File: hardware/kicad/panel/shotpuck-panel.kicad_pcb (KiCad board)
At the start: 2 copper layers, 91 x 92.6 mm, 291 parts, among them J1_0 TYPE-C 6PFS 2JCB1.6-H6.7 IPX8, J1_1 TYPE-C 6PFS 2JCB1.6-H6.7 IPX8, J1_2 TYPE-C 6PFS 2JCB1.6-H6.7 IPX8, J1_3 TYPE-C 6PFS 2JCB1.6-H6.7 IPX8, J2_0 SWD pads, J2_1 SWD pads, J2_2 SWD pads, J2_3 SWD pads, Q1_0 DMN63D8LDW, Q1_1 DMN63D8LDW, Q1_2 DMN63D8LDW, Q1_3 DMN63D8LDW, Q2_0 DMN2004DWK, Q2_1 DMN2004DWK, Q2_2 DMN2004DWK, Q2_3 DMN2004DWK, U1_0 BMD-340-A-R, U1_1 BMD-340-A-R, U1_2 BMD-340-A-R, U1_3 BMD-340-A-R, U2_0 LSM6DSO32TR, U2_1 LSM6DSO32TR, U2_2 LSM6DSO32TR, U2_3 LSM6DSO32TR, U3_0 MCP73831T-2ACI/OT, U3_1 MCP73831T-2ACI/OT, U3_2 MCP73831T-2ACI/OT, U3_3 MCP73831T-2ACI/OT, U4_0 BQ29700DSER, U4_1 BQ29700DSER, U4_2 BQ29700DSER, U4_3 BQ29700DSER

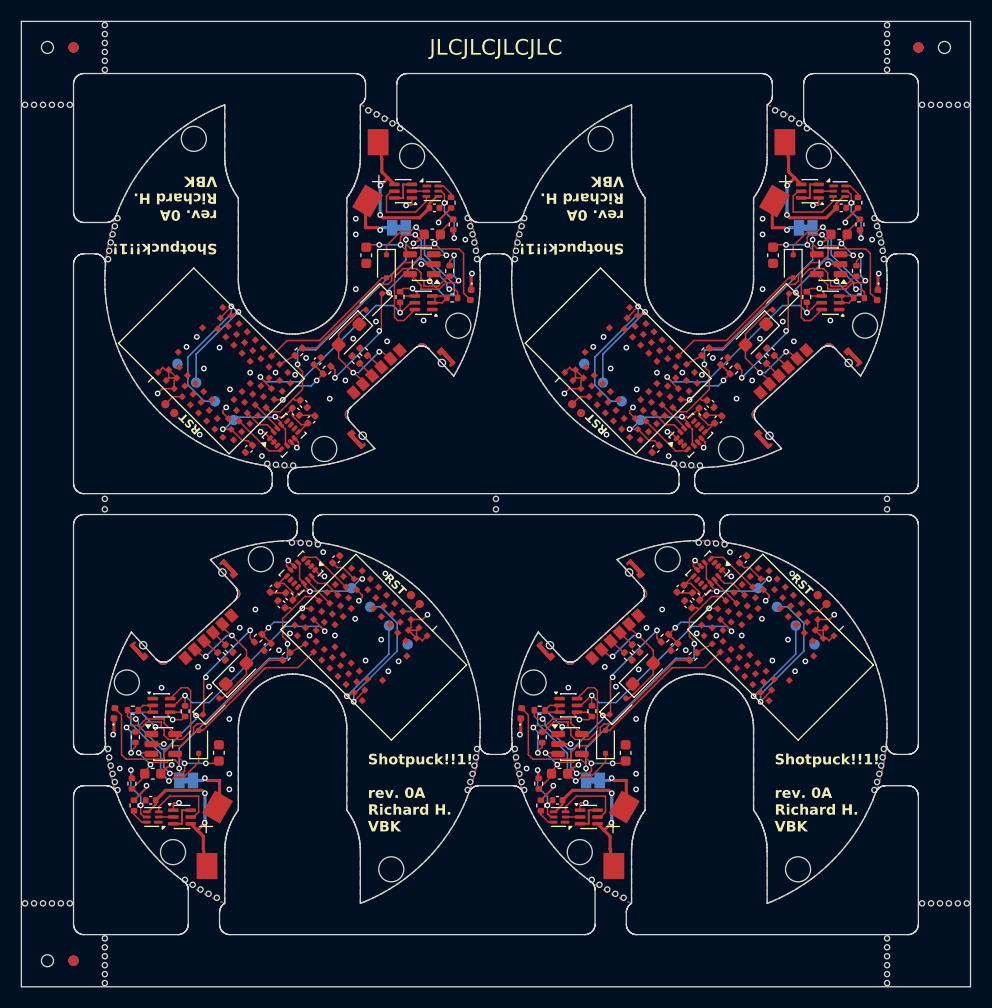
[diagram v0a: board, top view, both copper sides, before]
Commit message: Loose bolt tube under a cap lip, plate drawing, refreshed panel gerbers
Port main's loose-tube change (README D21) to the USB-C cap: the tube stands
on the plate and its top end sits in a ring lip under the cap top; the bolt
passes the cap top through a 8.4 mm hole. Tube 6.7 mm, puck 15.86 g. The
Blender bolt now sits on the cap top and the tube drops onto the plate.

Add mechanical/plate_drawing.py -> out/plate_drawing.pdf: hole table and the
M2x0.4 tapped-through callout for the plate order.

Regenerate the panel, its gerbers and the JLC BOM/CPL after the silkscreen
edit (panel DRC: 0 violations, 0 unconnected; BOM and CPL unchanged).

Co-Authored-By: Claude Opus 5.5 <noreply@anthropic.com>
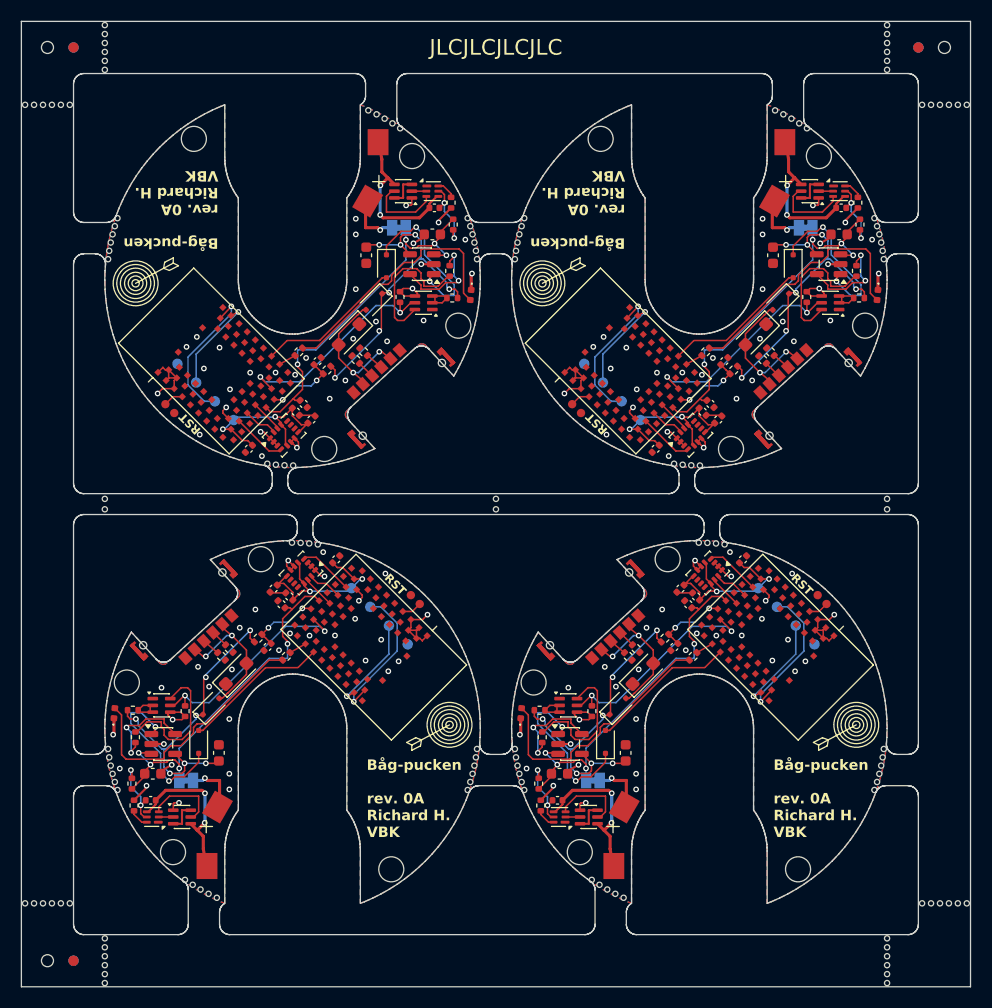
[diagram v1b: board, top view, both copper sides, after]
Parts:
- removed KiKit_MB_10_1, KiKit_MB_12_5, KiKit_MB_12_6, KiKit_MB_14_1, KiKit_MB_16_5, KiKit_MB_16_6, KiKit_MB_2_1, KiKit_MB_4_5, KiKit_MB_4_6, KiKit_MB_6_1, KiKit_MB_8_5, KiKit_MB_8_6: NPTH, NPTH
- added KiKit_MB_10_5: NPTH, NPTH, F.Cu at (119.4, 102.8)
- added KiKit_MB_10_6: NPTH, NPTH, F.Cu at (118.7, 102.3)
- added KiKit_MB_12_1: NPTH, NPTH, F.Cu at (128.9, 70.0)
- added KiKit_MB_14_5: NPTH, NPTH, F.Cu at (158.4, 102.8)
- added KiKit_MB_14_6: NPTH, NPTH, F.Cu at (157.7, 102.3)
- added KiKit_MB_16_1: NPTH, NPTH, F.Cu at (167.9, 70.0)
- added KiKit_MB_2_5: NPTH, NPTH, F.Cu at (138.6, 29.8)
- added KiKit_MB_2_6: NPTH, NPTH, F.Cu at (139.3, 30.2)
- added KiKit_MB_4_1: NPTH, NPTH, F.Cu at (129.1, 62.6)
- added KiKit_MB_6_5: NPTH, NPTH, F.Cu at (177.6, 29.8)
- added KiKit_MB_6_6: NPTH, NPTH, F.Cu at (178.3, 30.2)
- added KiKit_MB_8_1: NPTH, NPTH, F.Cu at (168.1, 62.6)
- moved KiKit_MB_19_2 75.0 mm to (186.0, 65.8)
- moved KiKit_MB_19_3 75.0 mm to (186.0, 66.8)
- moved KiKit_MB_17_2 37.5 mm to (111.0, 65.8)
- moved KiKit_MB_17_3 37.5 mm to (111.0, 66.8)
- moved KiKit_MB_18_2 37.5 mm to (148.5, 65.8)
- moved KiKit_MB_18_3 37.5 mm to (148.5, 66.8)
- moved KiKit_MB_14_2 35.0 mm to (160.7, 104.0)
- moved KiKit_MB_16_2 35.0 mm to (168.8, 70.0)
- moved KiKit_MB_10_2 35.0 mm to (121.7, 104.0)
- moved KiKit_MB_12_2 35.0 mm to (129.8, 70.0)
- moved KiKit_MB_6_2 35.0 mm to (175.3, 28.5)
- moved KiKit_MB_8_2 35.0 mm to (167.2, 62.6)
- moved KiKit_MB_2_2 35.0 mm to (136.3, 28.5)
- moved KiKit_MB_4_2 35.0 mm to (128.2, 62.6)
- moved KiKit_MB_14_3 35.0 mm to (159.9, 103.6)
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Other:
- board text added: "Båg-pucken rev. 0A Richard H. VBK"
- board text removed: "Shotpuck!!1! rev. 0A Richard H. VBK"

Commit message: Update ShotPuck specifications and design files for USB-C integration
- Adjusted dimensions: puck diameter increased to Ø40 × 10.43 mm, with 1.6 mm free space above the cell.
- Updated IMU to ST LSM6DSO32XTR, reflecting changes in the BOM and design files.
- Revised PCB thickness from 0.8 mm to 1.2 mm, ensuring compatibility with new components.
- Enhanced layout.json and README.md to reflect the latest design specifications and assembly details.
- Removed obsolete components and updated the BOM for JLCPCB assembly.
- Regenerated fabrication files, including gerbers and BOM, to align with the latest design changes.

Co-Authored-By: Claude Opus 5.5 <noreply@anthropic.com>
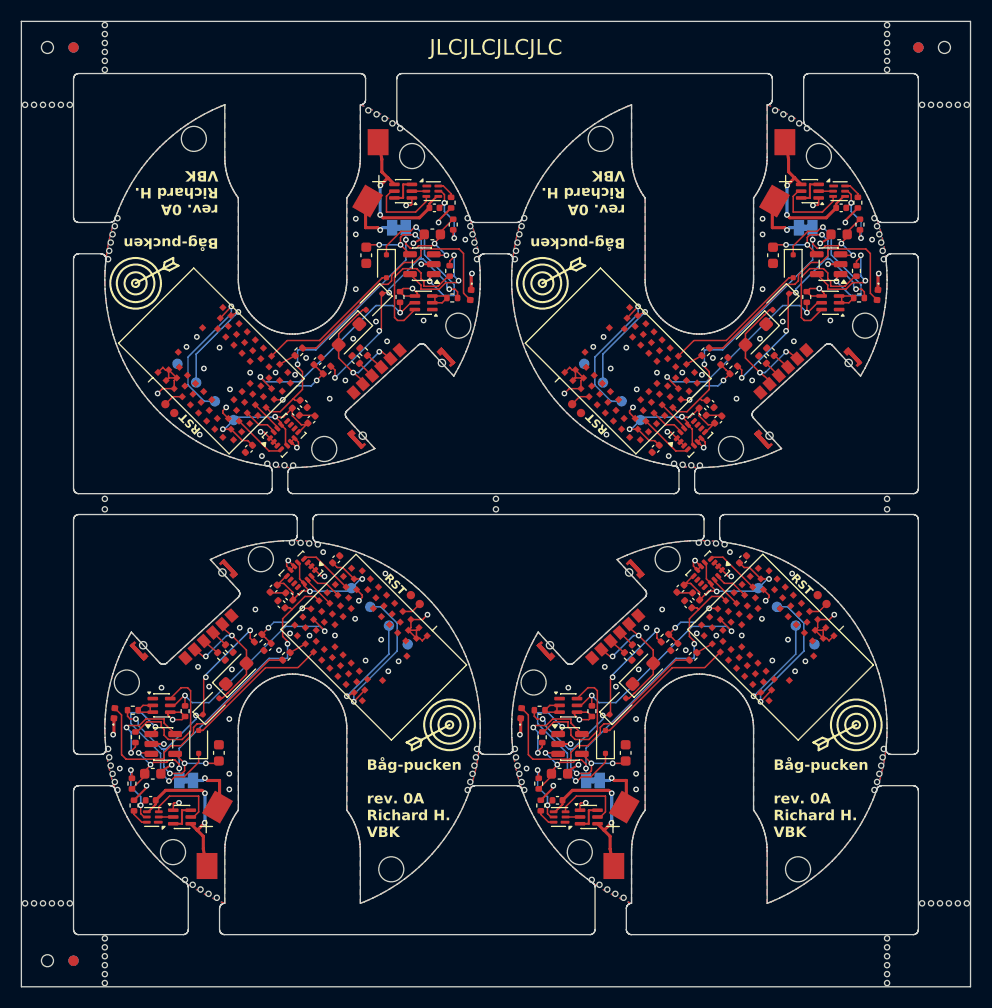
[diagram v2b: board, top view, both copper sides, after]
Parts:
- removed KiKit_MB_11_5, KiKit_MB_11_6, KiKit_MB_15_5, KiKit_MB_15_6, KiKit_MB_3_5, KiKit_MB_3_6, KiKit_MB_7_5, KiKit_MB_7_6: NPTH, NPTH
- added KiKit_MB_12_5: NPTH, NPTH, F.Cu at (111.4, 90.6)
- added KiKit_MB_12_6: NPTH, NPTH, F.Cu at (111.3, 89.8)
- added KiKit_MB_16_5: NPTH, NPTH, F.Cu at (150.4, 90.6)
- added KiKit_MB_16_6: NPTH, NPTH, F.Cu at (150.3, 89.8)
- added KiKit_MB_4_5: NPTH, NPTH, F.Cu at (146.6, 42.0)
- added KiKit_MB_4_6: NPTH, NPTH, F.Cu at (146.7, 42.8)
- added KiKit_MB_8_5: NPTH, NPTH, F.Cu at (185.6, 42.0)
- added KiKit_MB_8_6: NPTH, NPTH, F.Cu at (185.7, 42.8)
- U2_0, U2_1, U2_2, U2_3: value LSM6DSO32TR -> LSM6DSO32XTR
- moved KiKit_MB_19_2 75.0 mm to (111.0, 65.8)
- moved KiKit_MB_19_3 75.0 mm to (111.0, 66.8)
- moved KiKit_MB_17_2 37.5 mm to (148.5, 66.8)
- moved KiKit_MB_17_3 37.5 mm to (148.5, 65.8)
- moved KiKit_MB_18_2 37.5 mm to (186.0, 65.8)
- moved KiKit_MB_18_3 37.5 mm to (186.0, 66.8)
- moved KiKit_MB_13_3 34.7 mm to (185.4, 91.4)
- moved KiKit_MB_13_4 34.7 mm to (185.3, 92.1)
- moved KiKit_MB_5_3 34.7 mm to (150.6, 41.2)
- moved KiKit_MB_5_4 34.7 mm to (150.7, 40.4)
- moved KiKit_MB_1_3 34.7 mm to (111.6, 41.2)
- moved KiKit_MB_1_4 34.7 mm to (111.7, 40.4)
- moved KiKit_MB_9_3 34.7 mm to (146.4, 91.4)
- moved KiKit_MB_9_4 34.7 mm to (146.3, 92.1)
- moved KiKit_MB_13_2 34.7 mm to (185.6, 90.6)
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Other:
- outline, holes or cut-outs redrawn

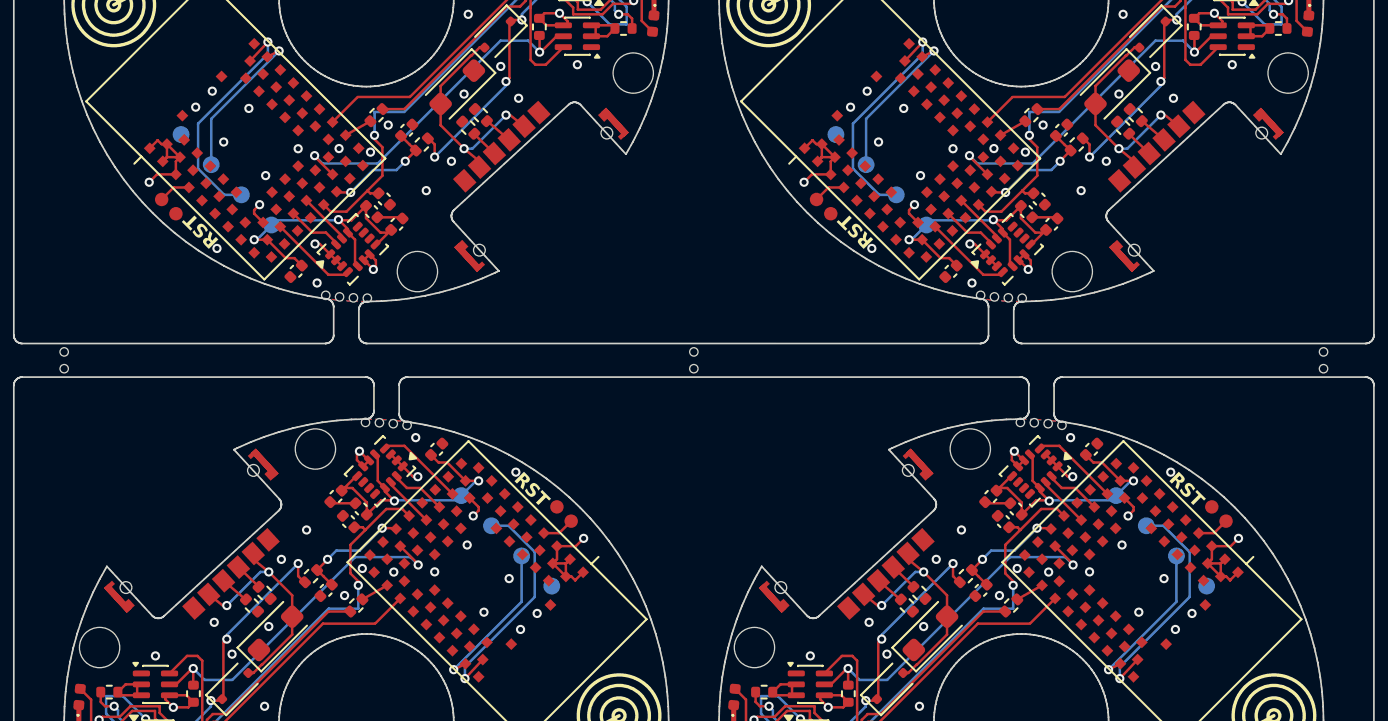
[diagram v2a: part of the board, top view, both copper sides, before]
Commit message: Update HANDOVER and README for recent design changes
- Enhanced J1's wing-tab pads for USB-C, increasing their area for better soldering.
- Adjusted D3's orientation in the CPL to match JLC's numbering.
- Added order package details in README for JLCPCB, including ORDER.md for order settings and checks.
- Regenerated fabrication files to reflect the latest design updates.

Co-Authored-By: Claude Opus 5.5 <noreply@anthropic.com>
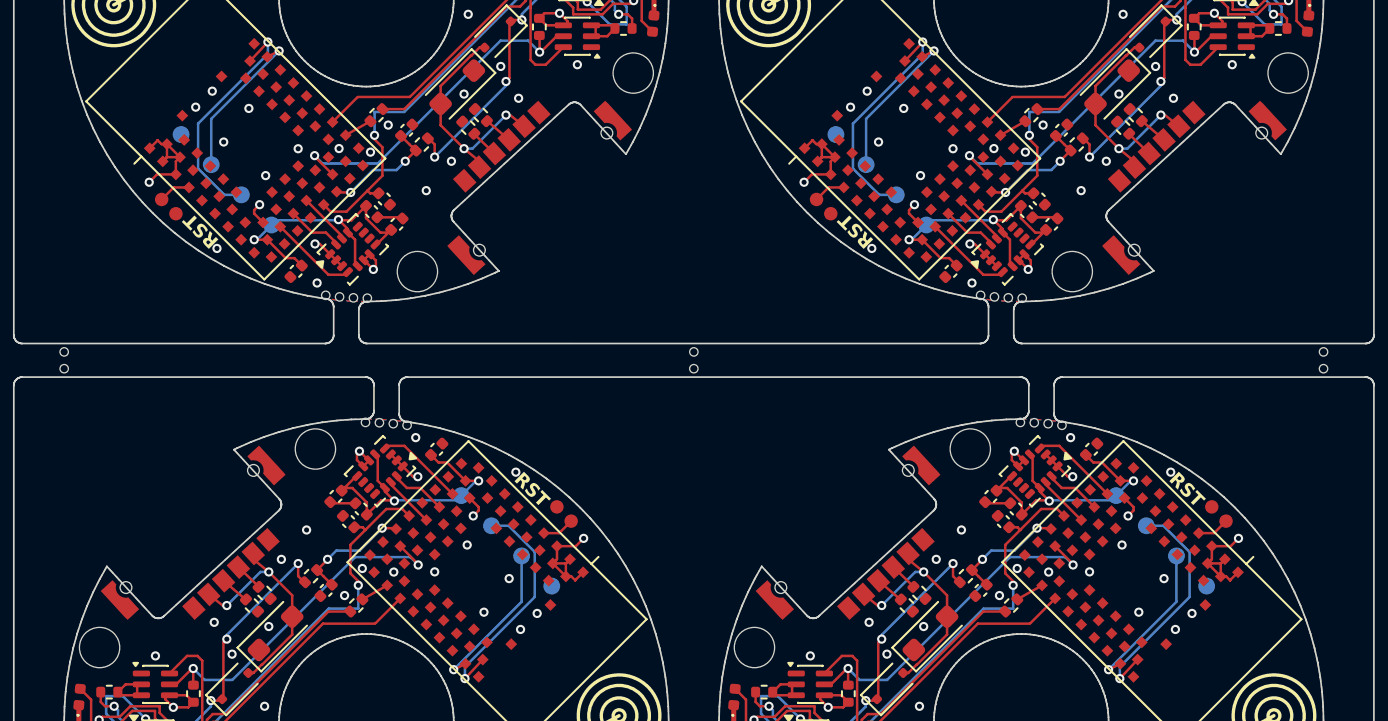
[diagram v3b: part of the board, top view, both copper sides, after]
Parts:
- removed KiKit_MB_10_5, KiKit_MB_10_6, KiKit_MB_11_1, KiKit_MB_14_5, KiKit_MB_14_6, KiKit_MB_15_1, KiKit_MB_2_5, KiKit_MB_2_6, KiKit_MB_3_1, KiKit_MB_6_5, KiKit_MB_6_6, KiKit_MB_7_1: NPTH, NPTH
- added KiKit_MB_10_1: NPTH, NPTH, F.Cu at (128.9, 70.0)
- added KiKit_MB_11_5: NPTH, NPTH, F.Cu at (119.4, 102.8)
- added KiKit_MB_11_6: NPTH, NPTH, F.Cu at (118.7, 102.3)
- added KiKit_MB_14_1: NPTH, NPTH, F.Cu at (167.9, 70.0)
- added KiKit_MB_15_5: NPTH, NPTH, F.Cu at (158.4, 102.8)
- added KiKit_MB_15_6: NPTH, NPTH, F.Cu at (157.7, 102.3)
- added KiKit_MB_2_1: NPTH, NPTH, F.Cu at (129.1, 62.6)
- added KiKit_MB_3_5: NPTH, NPTH, F.Cu at (138.6, 29.8)
- added KiKit_MB_3_6: NPTH, NPTH, F.Cu at (139.3, 30.2)
- added KiKit_MB_6_1: NPTH, NPTH, F.Cu at (168.1, 62.6)
- added KiKit_MB_7_5: NPTH, NPTH, F.Cu at (177.6, 29.8)
- added KiKit_MB_7_6: NPTH, NPTH, F.Cu at (178.3, 30.2)
- moved KiKit_MB_14_2 35.0 mm to (168.8, 70.0)
- moved KiKit_MB_15_2 35.0 mm to (160.7, 104.0)
- moved KiKit_MB_10_2 35.0 mm to (129.8, 70.0)
- moved KiKit_MB_11_2 35.0 mm to (121.7, 104.0)
- moved KiKit_MB_6_2 35.0 mm to (167.2, 62.6)
- moved KiKit_MB_7_2 35.0 mm to (175.3, 28.5)
- moved KiKit_MB_2_2 35.0 mm to (128.2, 62.6)
- moved KiKit_MB_3_2 35.0 mm to (136.3, 28.5)
- moved KiKit_MB_14_3 35.0 mm to (169.6, 70.1)
- moved KiKit_MB_15_3 35.0 mm to (159.9, 103.6)
- moved KiKit_MB_10_3 35.0 mm to (130.6, 70.1)
- moved KiKit_MB_11_3 35.0 mm to (120.9, 103.6)
- moved KiKit_MB_6_3 35.0 mm to (166.4, 62.5)
- moved KiKit_MB_7_3 35.0 mm to (176.1, 28.9)
- moved KiKit_MB_2_3 35.0 mm to (127.4, 62.5)
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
